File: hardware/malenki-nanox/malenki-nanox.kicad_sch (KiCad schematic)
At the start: 25 parts, among them J1 Conn_01x02_Male, J2 Conn_01x08_Male, J3 Conn_01x02, J5 Conn_01x02_Male, J6 Conn_01x02_Male, J7 Conn_01x02_Male, U1 A7105-MODULE, U2 AIC1734-33GUTR, U3 ATtiny1617-M, U5 DRV8837DSGR, U6 DRV8837DSGR, U7 DRV8837DSGR

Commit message: Update to latest kicad 6
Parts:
- D1, D2: footprint LED_SMD:LED_0805_2012Metric_Castellated -> LED_SMD:LED_0805_2012Metric_Pad1.15x1.40mm_HandSolder

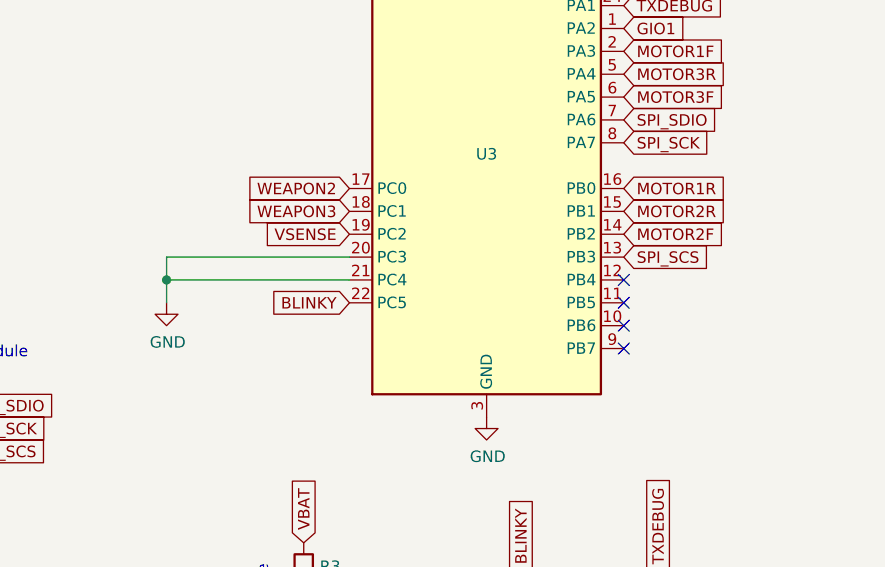
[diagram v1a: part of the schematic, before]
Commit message: Minor board update layout: add vsense on pin PB5
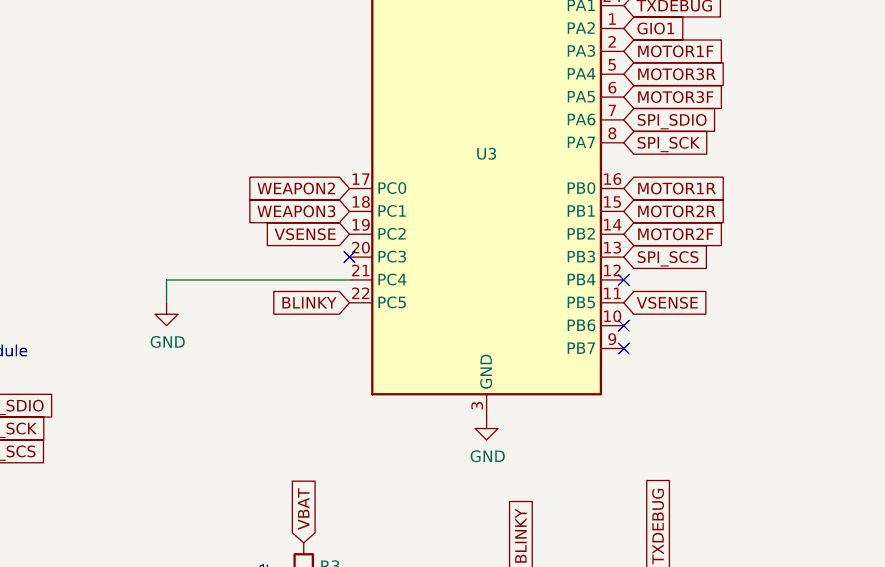
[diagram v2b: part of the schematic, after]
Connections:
- net GND: no longer U3.20 (PC3)
- net VSENSE: now also U3.11 (PB5)
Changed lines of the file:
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@@
   (junction (at 63.5 55.88) (diameter 1.016) (color 0 0 0 0))
   (junction (at 78.74 55.88) (diameter 1.016) (color 0 0 0 0))
-  (junction (at 91.44 119.38) (diameter 1.016) (color 0 0 0 0))
   (junction (at 92.71 48.26) (diameter 1.016) (color 0 0 0 0))
   (junction (at 106.68 156.21) (diameter 1.016) (color 0 0 0 0))
@@
   (junction (at 219.71 53.34) (diameter 1.016) (color 0 0 0 0))
   (no_connect (at 38.1 140.97))
+  (no_connect (at 111.76 116.84))
   (no_connect (at 129.54 48.26))
   (no_connect (at 129.54 53.34))
@@
   (no_connect (at 129.54 60.96))
   (no_connect (at 142.24 119.38))
-  (no_connect (at 142.24 121.92))
   (no_connect (at 142.24 124.46))
   (no_connect (at 142.24 127))
@@
     (stroke (width 0) (type solid) (color 0 0 0 0))
   )
-  (wire (pts (xy 91.44 116.84) (xy 91.44 119.38))
-    (stroke (width 0) (type solid) (color 0 0 0 0))
-  )
-  (wire (pts (xy 91.44 116.84) (xy 111.76 116.84))
-    (stroke (width 0) (type solid) (color 0 0 0 0))
-  )
   (wire (pts (xy 91.44 119.38) (xy 91.44 121.92))
     (stroke (width 0) (type solid) (color 0 0 0 0))
@@
       (effects (font (size 1.27 1.27)) hide)
     )
+  )
+  (global_label "VSENSE" (shape input) (at 142.24 121.92 0)
+    (effects (font (size 1.27 1.27)) (justify left))
+    (property "Intersheet References" "${INTERSHEET_REFS}" (id 0) (at 254 236.22 0)
+      (effects (font (size 1.27 1.27)) hide)
+    )

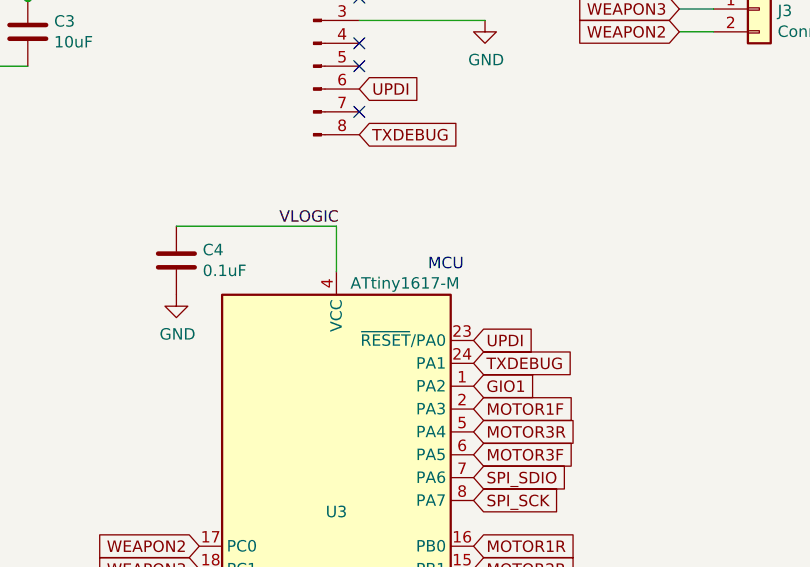
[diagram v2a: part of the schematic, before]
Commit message: Update part number for tiny817
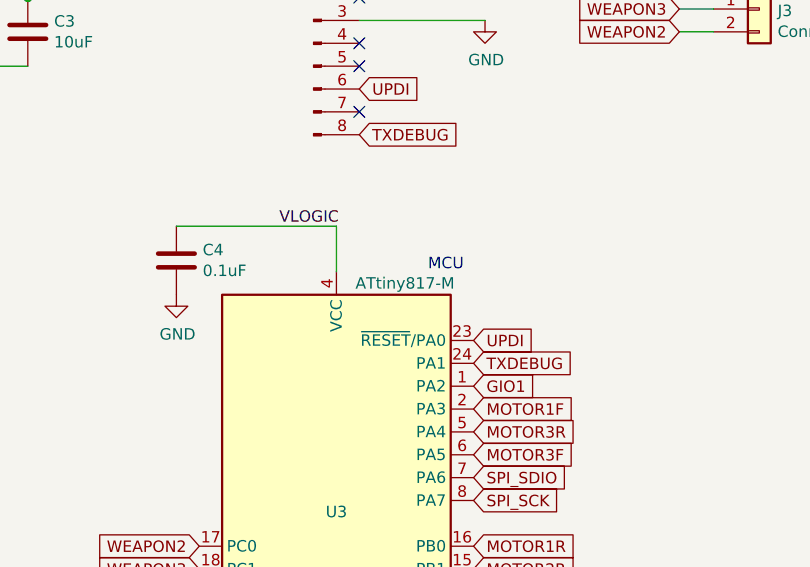
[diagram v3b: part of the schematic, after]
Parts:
- U3: value ATtiny1617-M -> ATtiny817-M; LCSC C194193 -> (none); Partnum C194193 -> (none)
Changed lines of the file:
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@@
     (in_bom yes) (on_board yes)
     (property "Reference" "U3" (id 0) (at 127 105.41 0))
-    (property "Value" "ATtiny1617-M" (id 1) (at 134.62 80.01 0))
+    (property "Value" "ATtiny817-M" (id 1) (at 134.62 80.01 0))
     (property "Footprint" "malenki-nano:qfn24-hand1" (id 2) (at 127 106.68 0)
       (effects (font (size 1.27 1.27) italic) hide)
@@
       (effects (font (size 1.27 1.27)) hide)
     )
-    (property "Partnum" "C194193" (id 4) (at 127 106.68 0)
+    (property "Partnum" "" (id 4) (at 127 106.68 0)
       (effects (font (size 1.27 1.27)) hide)
     )
-    (property "LCSC" "C194193" (id 5) (at 127 106.68 0)
+    (property "LCSC" "" (id 5) (at 127 106.68 0)
       (effects (font (size 1.27 1.27)) hide)
     )
@@
     )
     (path "/00000000-0000-0000-0000-00005dc45560"
-      (reference "U3") (unit 1) (value "ATtiny1617-M") (footprint "malenki-nano:qfn24-hand1")
+      (reference "U3") (unit 1) (value "ATtiny817-M") (footprint "malenki-nano:qfn24-hand1")
     )
     (path "/00000000-0000-0000-0000-00005e3afae0"
